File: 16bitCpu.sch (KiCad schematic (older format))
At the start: 0 parts

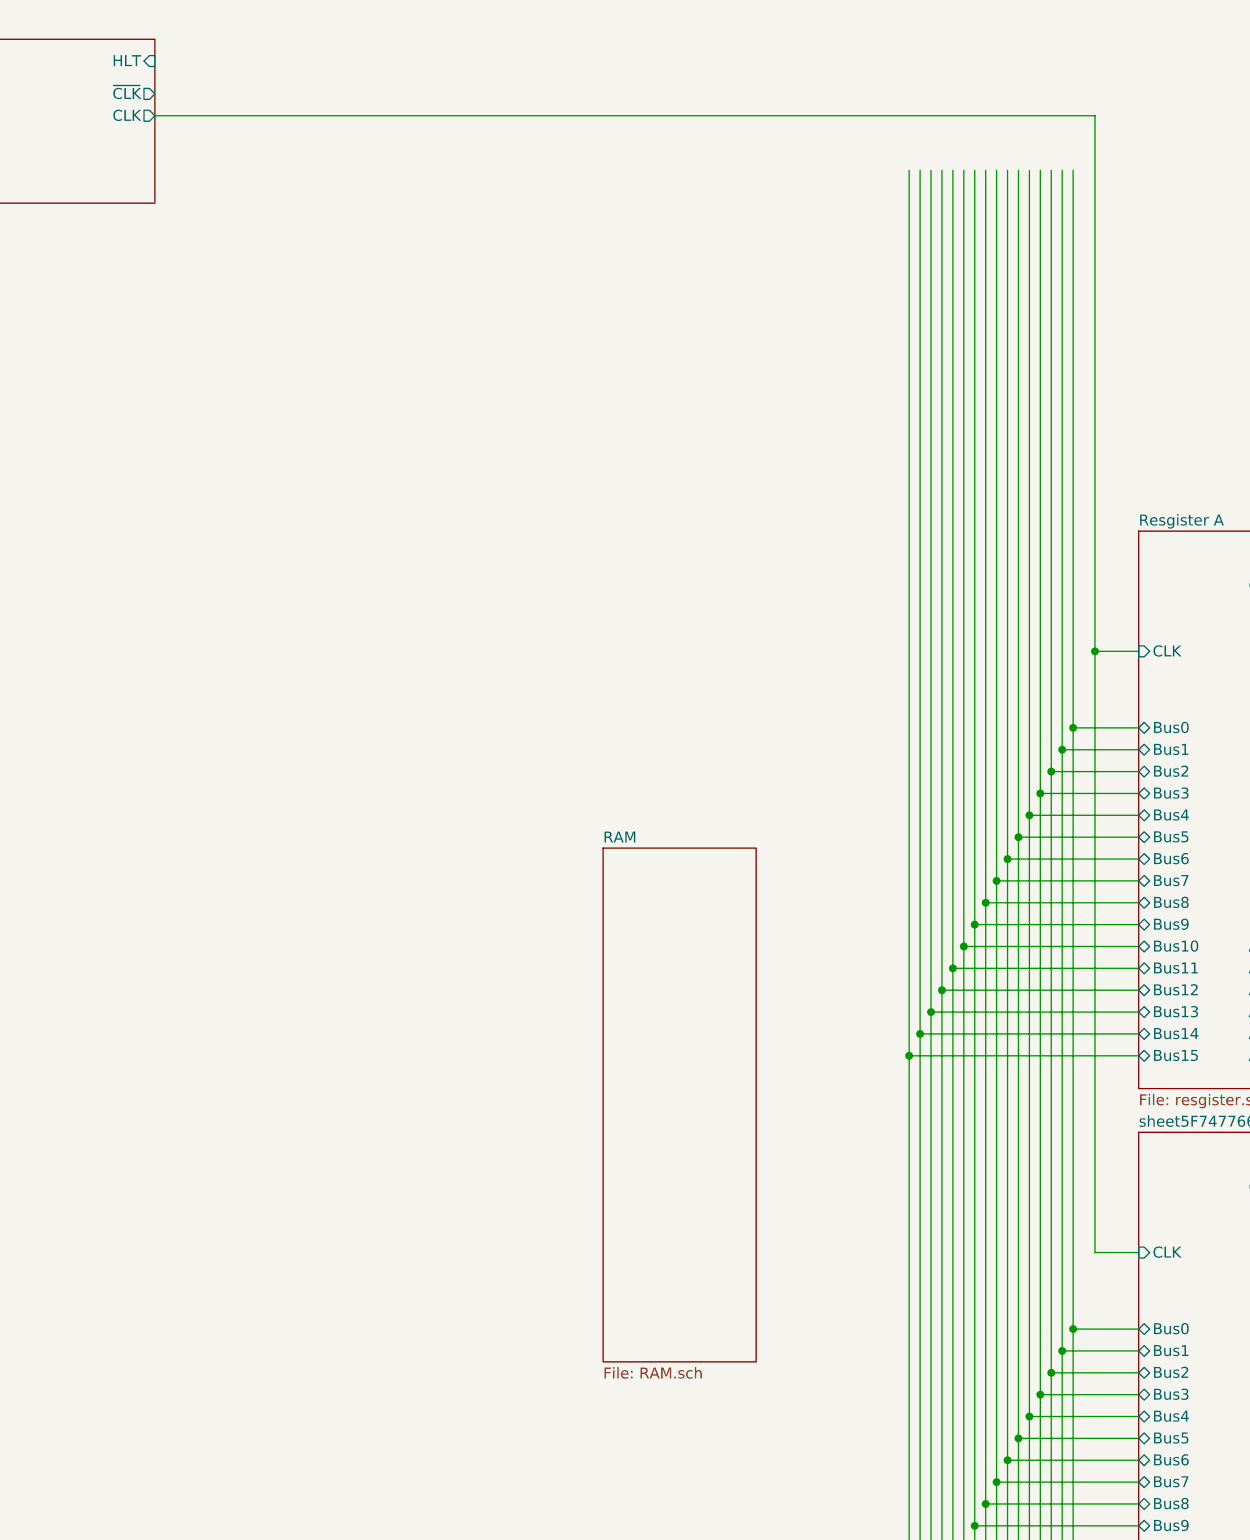
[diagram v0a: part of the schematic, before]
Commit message: ram connected,need to add and a cap
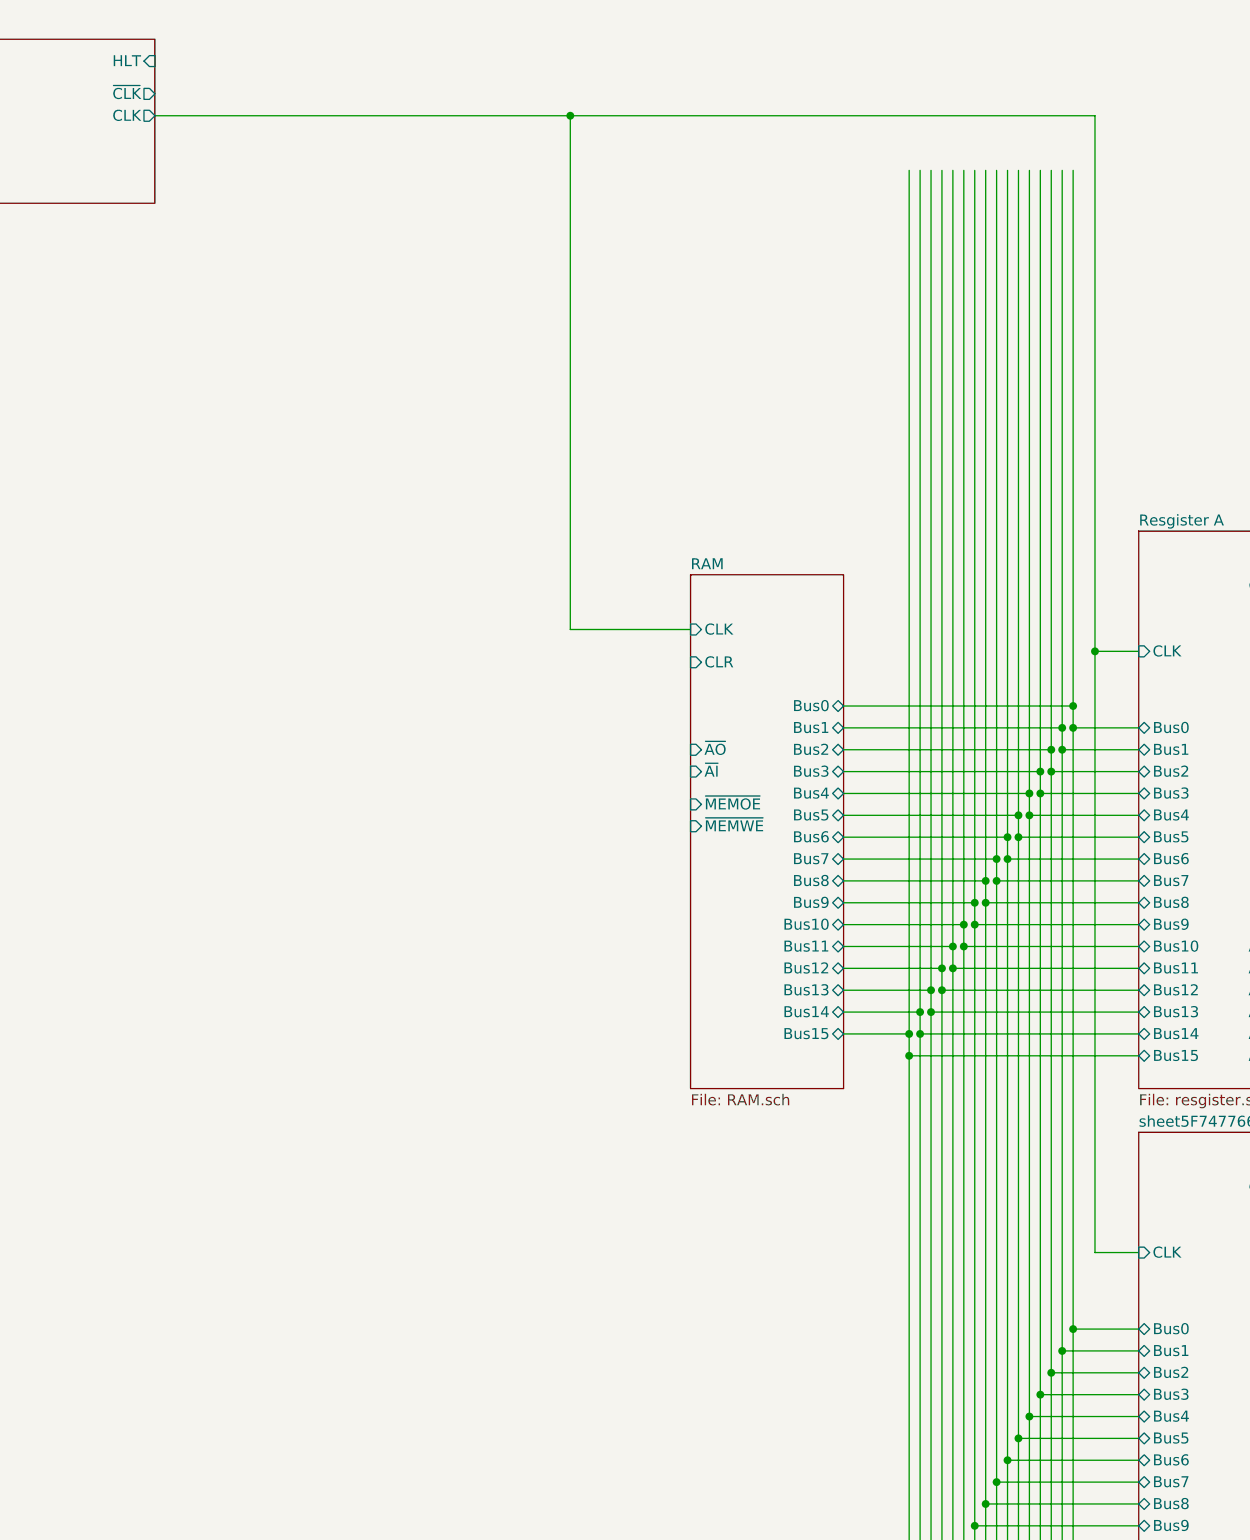
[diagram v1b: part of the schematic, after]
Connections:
- wire segments 213 -> 248
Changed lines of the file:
@@
 $EndDescr
 Wire Wire Line
-	8600 1300 8600 5250
-Wire Wire Line
-	8700 1300 8700 5050
-Wire Wire Line
-	8750 1300 8750 4950
-Wire Wire Line
-	8800 1300 8800 4850
-Wire Wire Line
-	8850 1300 8850 4750
-Wire Wire Line
-	8900 1300 8900 4650
-Wire Wire Line
-	8950 1300 8950 4550
-Wire Wire Line
-	9000 1300 9000 4450
-Wire Wire Line
-	9050 1300 9050 4350
-Wire Wire Line
-	9100 1300 9100 4250
-Wire Wire Line
-	9150 1300 9150 4150
-Wire Wire Line
-	9200 1300 9200 4050
-Wire Wire Line
-	9250 1300 9250 3950
+	8600 1300 8600 5150
+Wire Wire Line
+	8700 1300 8700 4950
+Wire Wire Line
+	8750 1300 8750 4850
+Wire Wire Line
+	8800 1300 8800 4750
+Wire Wire Line
+	8850 1300 8850 4650
+Wire Wire Line
+	8900 1300 8900 4550
+Wire Wire Line
+	8950 1300 8950 4450
+Wire Wire Line
+	9050 1300 9050 4250
+Wire Wire Line
+	9100 1300 9100 4150
+Wire Wire Line
+	9150 1300 9150 4050
+Wire Wire Line
+	9200 1300 9200 3950
+Wire Wire Line
+	9250 1300 9250 3850
 Wire Wire Line
 	9300 3850 9600 3850
@@
 Wire Wire Line
 	8650 5150 9600 5150
-Wire Wire Line
-	8650 1300 8650 5150
 Connection ~ 8650 5150
 Wire Wire Line
@@
 Connection ~ 8550 5350
 Wire Wire Line
-	8550 5350 8550 1300
+	8550 5350 8550 5250
 $Sheet
 S 11250 3450 850  3850
@@
 Wire Wire Line
 	9300 3850 9300 6600
-Wire Wire Line
-	9300 1300 9300 3850
 $Sheet
 S 9600 2950 700  2550
@@
 $EndSheet
 Wire Wire Line
-	5100 1050 9400 1050
+	5100 1050 7000 1050
 Wire Wire Line
 	9400 1050 9400 3500
@@
 Connection ~ 9400 3500
 $Sheet
-S 7150 4400 700  2350
+S 7550 3150 700  2350
 U 5F681977
 F0 "RAM" 50
 F1 "RAM.sch" 50
+F2 "CLK" I L 7550 3400 50
+F3 "Bus0" T R 8250 3750 50
+F4 "~AO" I L 7550 3950 50
+F5 "CLR" I L 7550 3550 50
+F6 "Bus1" T R 8250 3850 50
+F7 "Bus2" T R 8250 3950 50
+F8 "Bus3" T R 8250 4050 50
+F9 "Bus4" T R 8250 4150 50
+F10 "Bus5" T R 8250 4250 50
+F11 "Bus6" T R 8250 4350 50
+F12 "Bus7" T R 8250 4450 50
+F13 "Bus8" T R 8250 4550 50
+F14 "Bus9" T R 8250 4650 50
+F15 "Bus10" T R 8250 4750 50
+F16 "Bus11" T R 8250 4850 50
+F17 "Bus12" T R 8250 4950 50
+F18 "Bus13" T R 8250 5050 50
+F19 "Bus14" T R 8250 5150 50
+F20 "Bus15" T R 8250 5250 50
+F21 "~AI" I L 7550 4050 50
+F22 "~MEMOE" I L 7550 4200 50
+F23 "~MEMWE" I L 7550 4300 50
 $EndSheet
+Wire Wire Line
+	9300 1300 9300 3750
+Wire Wire Line
+	8250 3750 9300 3750
+Connection ~ 9300 3750
+Wire Wire Line
+	9300 3750 9300 3850
+Wire Wire Line
+	8250 3850 9250 3850
+Connection ~ 9250 3850
+Wire Wire Line
+	9250 3850 9250 3950
+Wire Wire Line
+	8250 3950 9200 3950
+Connection ~ 9200 3950
+Wire Wire Line
+	9200 3950 9200 4050
+Wire Wire Line
+	8250 4050 9150 4050
+Connection ~ 9150 4050
+Wire Wire Line
+	9150 4050 9150 4150
+Wire Wire Line
+	8250 4150 9100 4150
+Connection ~ 9100 4150
+Wire Wire Line
+	9100 4150 9100 4250
+Wire Wire Line
+	8250 4250 9050 4250
+Connection ~ 9050 4250
+Wire Wire Line
+	9050 4250 9050 4350
+Wire Wire Line
+	8250 4350 9000 4350
+Wire Wire Line
+	9000 1300 9000 4350
+Connection ~ 9000 4350
+Wire Wire Line
+	9000 4350 9000 4450
+Wire Wire Line
+	8250 4450 8950 4450
+Connection ~ 8950 4450
+Wire Wire Line
+	8950 4450 8950 4550
+Wire Wire Line
+	8250 4550 8900 4550
+Connection ~ 8900 4550
+Wire Wire Line
+	8900 4550 8900 4650
+Wire Wire Line
+	8250 4650 8850 4650
+Connection ~ 8850 4650
+Wire Wire Line
+	8850 4650 8850 4750
+Wire Wire Line
+	8250 4750 8800 4750
+Connection ~ 8800 4750
+Wire Wire Line
+	8800 4750 8800 4850
+Wire Wire Line
+	8250 4850 8750 4850
+Connection ~ 8750 4850
+Wire Wire Line
+	8750 4850 8750 4950
+Wire Wire Line
+	8250 4950 8700 4950
+Connection ~ 8700 4950
+Wire Wire Line
+	8700 4950 8700 5050
+Wire Wire Line
+	8250 5050 8650 5050
+Wire Wire Line
+	8650 1300 8650 5050
+Connection ~ 8650 5050
+Wire Wire Line
+	8650 5050 8650 5150
+Wire Wire Line
+	8250 5150 8600 5150
+Connection ~ 8600 5150
+Wire Wire Line
+	8600 5150 8600 5250
+Wire Wire Line
+	8250 5250 8550 5250
+Connection ~ 8550 5250
+Wire Wire Line
+	8550 5250 8550 1300
+Wire Wire Line
+	7550 3400 7000 3400
+Wire Wire Line
+	7000 3400 7000 1050
+Connection ~ 7000 1050
+Wire Wire Line
+	7000 1050 9400 1050
 $EndSCHEMATC

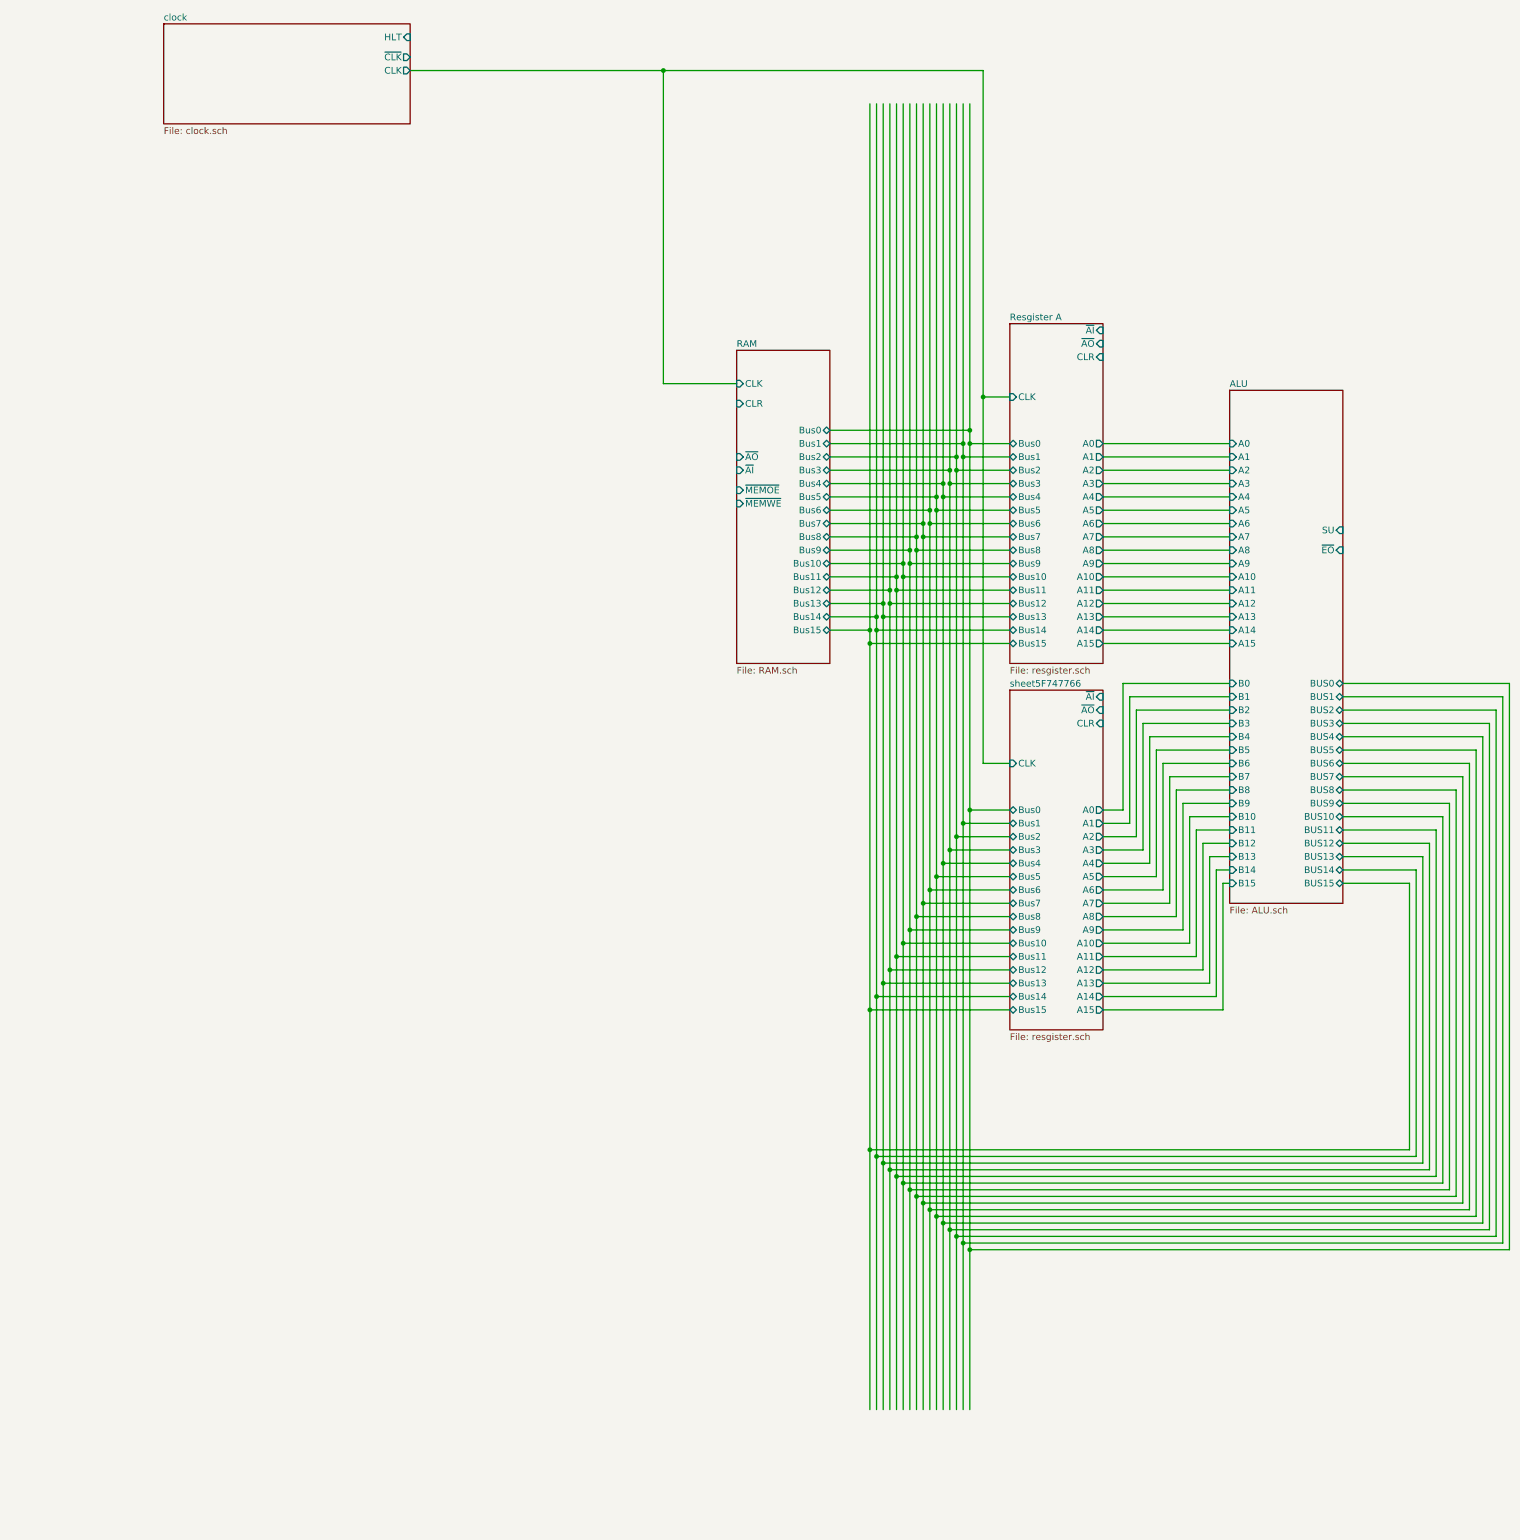
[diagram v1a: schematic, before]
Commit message: Added the program counter
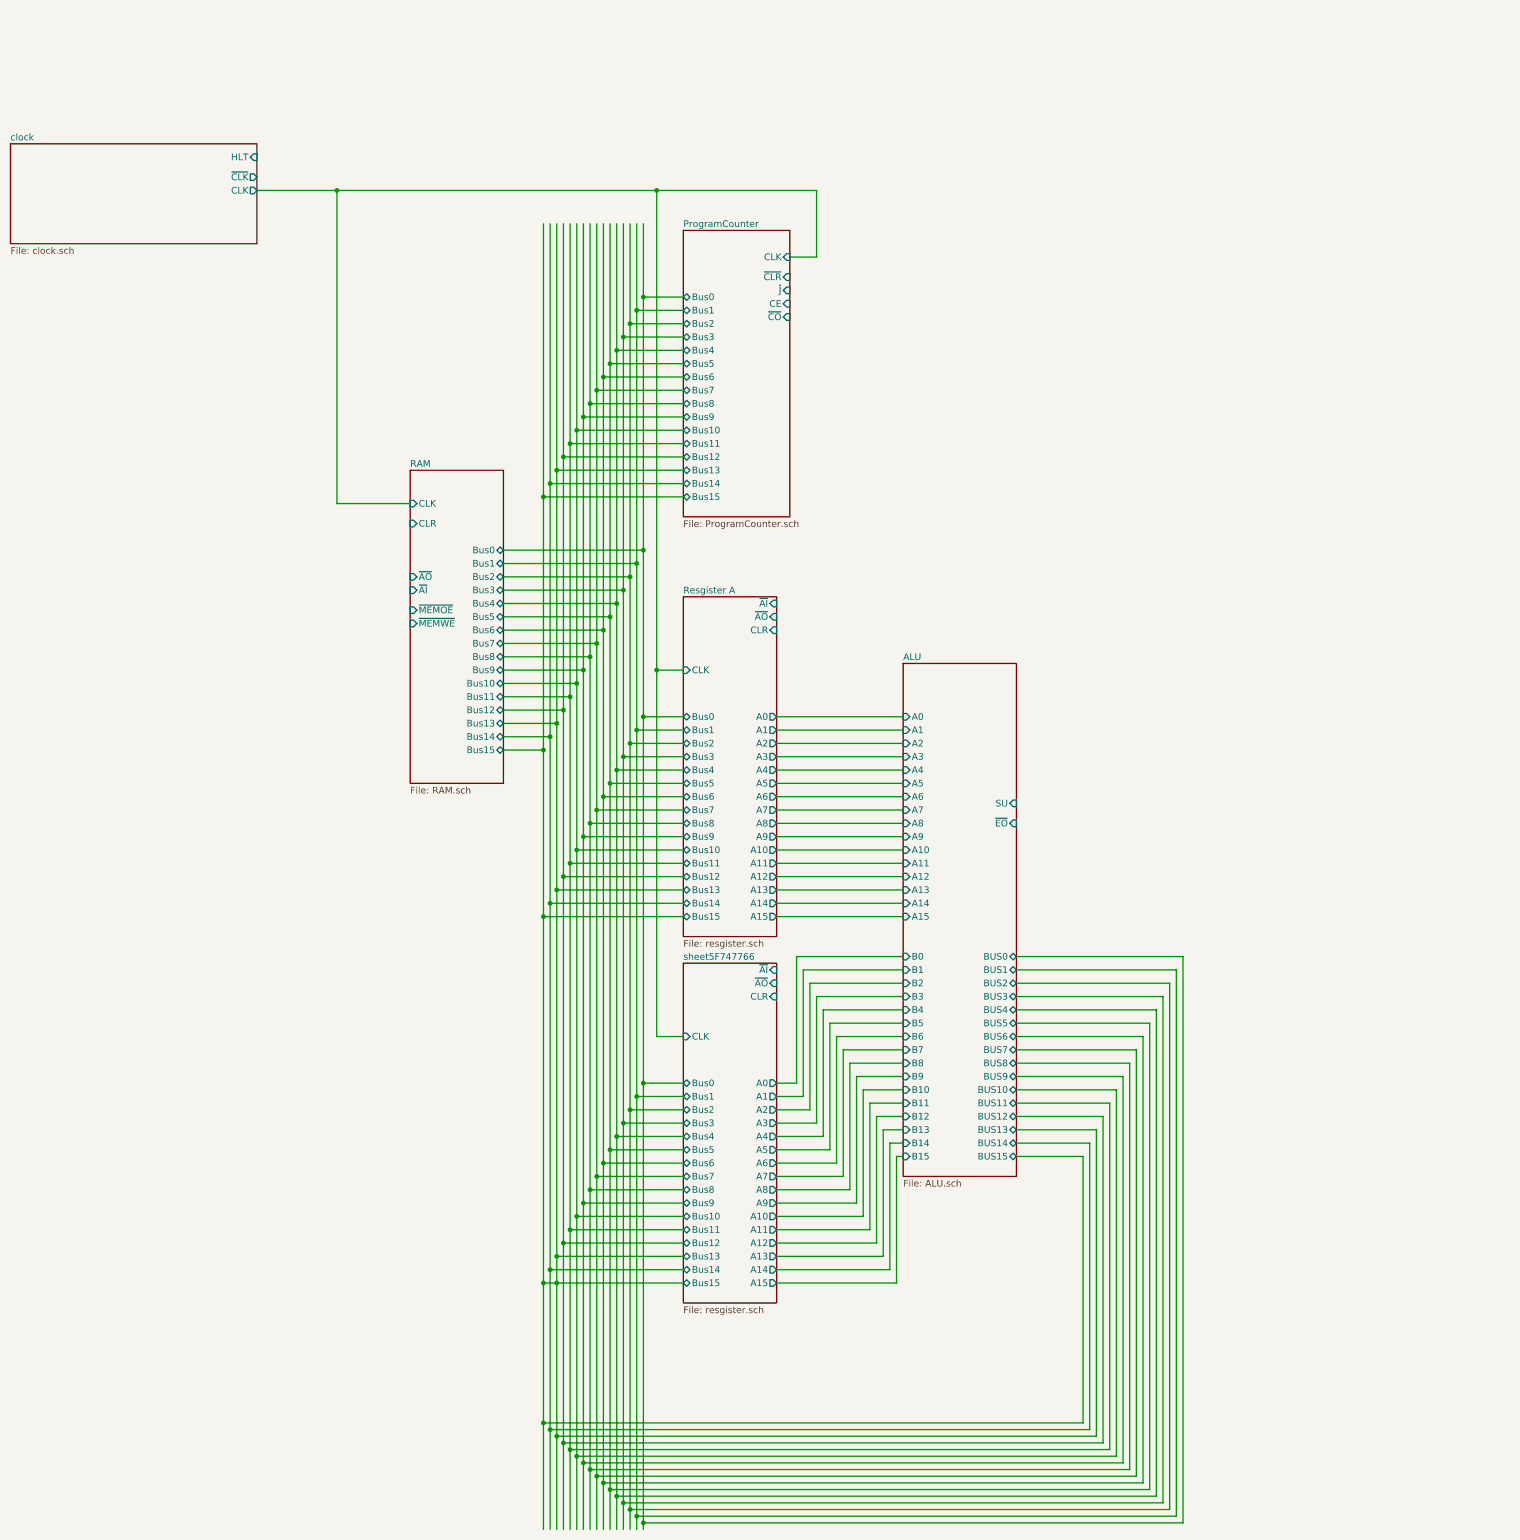
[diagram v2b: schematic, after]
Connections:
- wire segments 248 -> 285
